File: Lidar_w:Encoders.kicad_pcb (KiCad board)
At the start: 2 copper layers, 67 x 61.5 mm, 15 parts, among them J1 DB15_HighDensity_MountingHoles, J2 DB15_HighDensity_MountingHoles, P1 CONN_01X04, P2 CONN_01X04, P3 CONN_01X04, P4 CONN_01X04, P5 CONN_01X05, P6 CONN_01X04, U1 MCP2551-I/P, U2 Teensy3.6

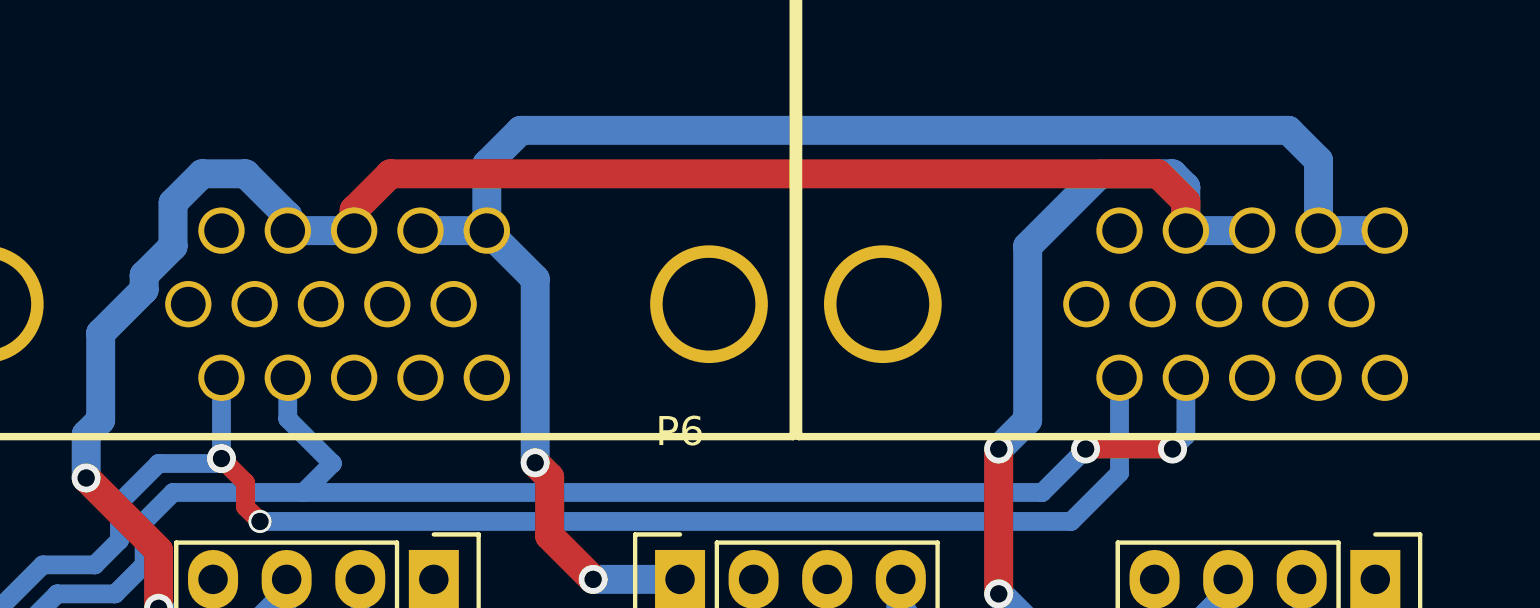
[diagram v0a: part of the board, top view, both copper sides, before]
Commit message: Took out VIAs; fixed fills.
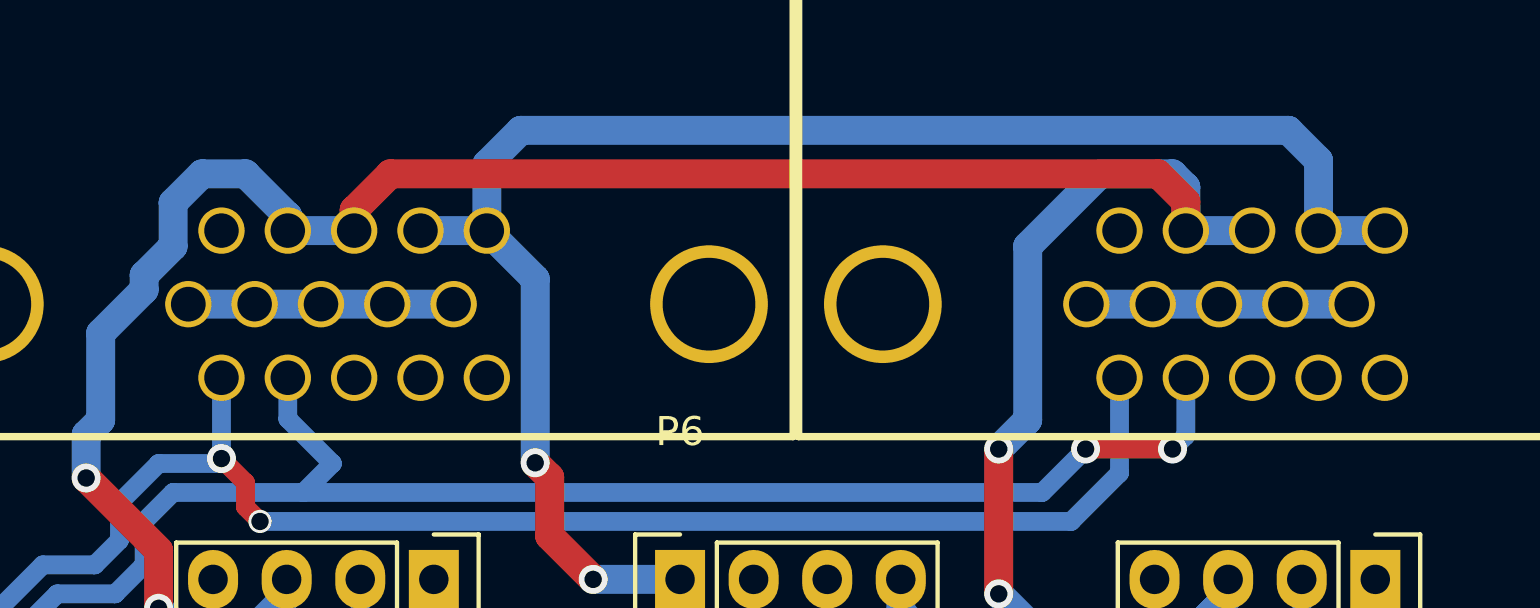
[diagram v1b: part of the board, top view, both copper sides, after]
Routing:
- net GND: track 0.00 -> 18.3 mm
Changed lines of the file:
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@@
   (general
     (links 62)
-    (no_connects 11)
+    (no_connects 3)
     (area 148.924999 75.146999 216.075001 143.385)
     (thickness 1.6)
     (drawings 11)
-    (tracks 250)
+    (tracks 258)
     (zones 0)
     (modules 15)
@@
   (gr_line (start 216 81.5) (end 216 140.5) (angle 90) (layer Edge.Cuts) (width 0.15))
   (gr_line (start 215 81.5) (end 216 81.5) (angle 90) (layer Edge.Cuts) (width 0.15))
+  (segment (start 191.525 93) (end 193.815 93) (width 1) (layer B.Cu) (net 1) (status C00000))
+  (segment (start 193.815 93) (end 196.105 93) (width 1) (layer B.Cu) (net 1) (status C00000))
+  (segment (start 196.105 93) (end 198.395 93) (width 1) (layer B.Cu) (net 1) (status C00000))
+  (segment (start 198.395 93) (end 200.685 93) (width 1) (layer B.Cu) (net 1) (status C00000))
+  (segment (start 160.525 93) (end 162.815 93) (width 1) (layer B.Cu) (net 1) (status C00000))
+  (segment (start 162.815 93) (end 165.105 93) (width 1) (layer B.Cu) (net 1) (status C00000))
+  (segment (start 165.105 93) (end 167.395 93) (width 1) (layer B.Cu) (net 1) (status C00000))
+  (segment (start 167.395 93) (end 169.685 93) (width 1) (layer B.Cu) (net 1) (status C00000))
   (segment (start 192 135) (end 192 136.5) (width 0.65) (layer B.Cu) (net 2) (status 10))
   (segment (start 199.54 136.46) (end 199.54 135) (width 0.65) (layer B.Cu) (net 2) (status 20))
